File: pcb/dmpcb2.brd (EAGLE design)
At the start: 100 x 100 mm, 70 parts, among them IC1 7805DT, IC2 L293D, IC4 LM358D, IC5 LM358D, J7 SJ-3523-SMT-TR, Q1 IRF530, Q2 IRF530

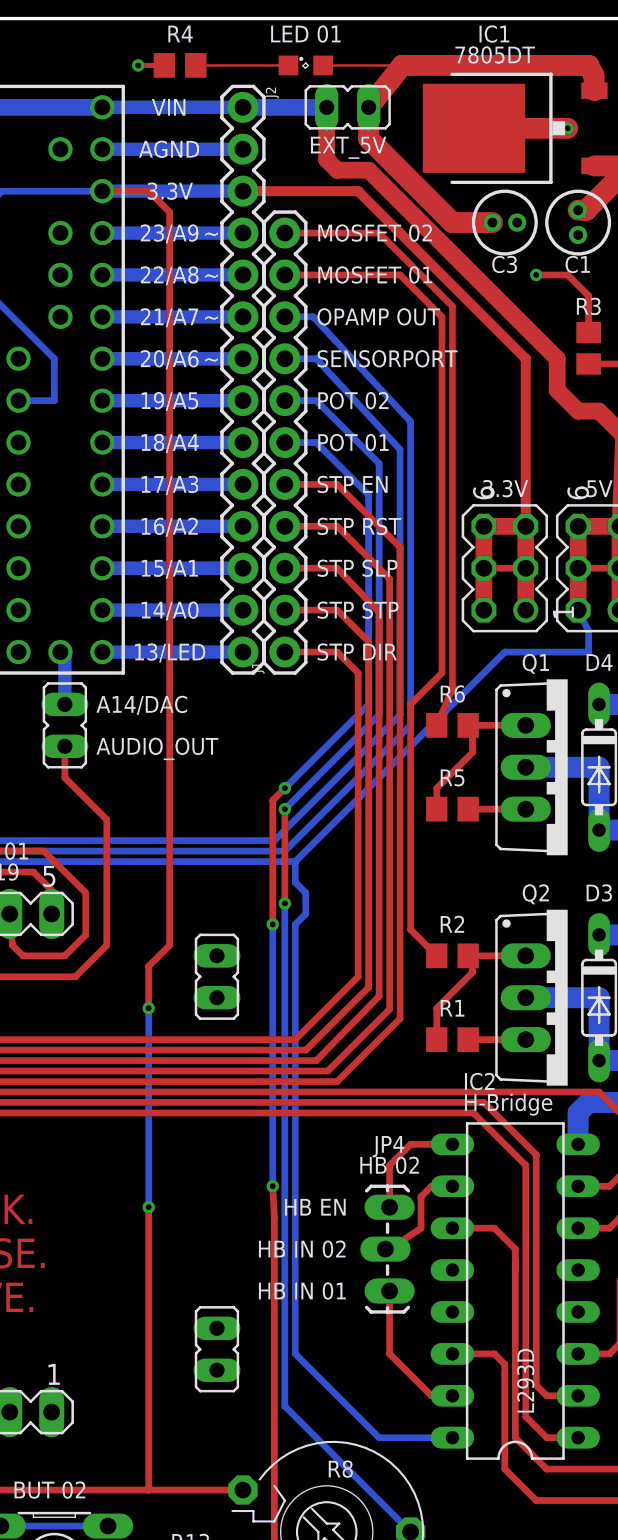
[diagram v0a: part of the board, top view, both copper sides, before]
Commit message: fixed some wire stubs
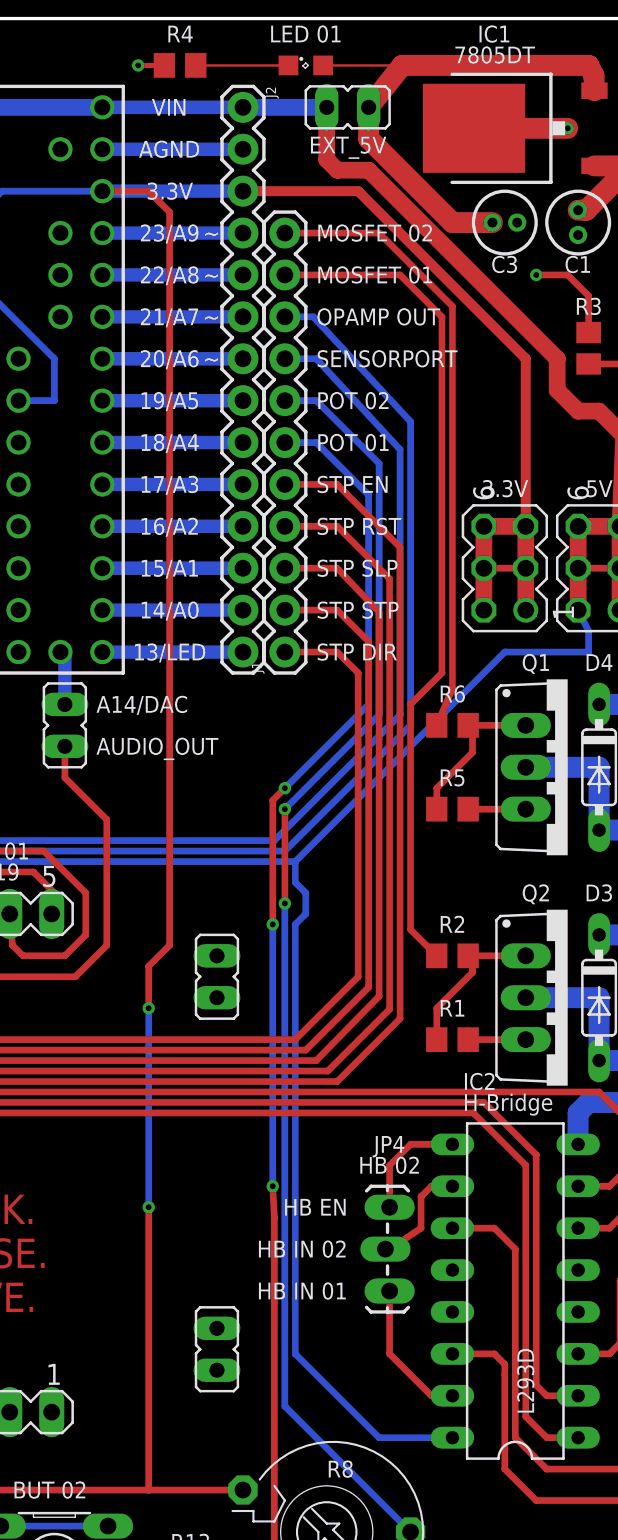
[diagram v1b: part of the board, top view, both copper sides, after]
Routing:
- net +5V: track 359.2 -> 358.0 mm
- net N$12: track 29.5 -> 28.8 mm
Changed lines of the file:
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@@
 <wire x1="89.756784375" y1="74.708215625" x2="89.756784375" y2="74.67648125" width="1.016" layer="1"/>
 <wire x1="89.756784375" y1="74.67648125" x2="89.535" y2="69.215" width="1.016" layer="1"/>
-<wire x1="71.755" y1="94.615" x2="71.755" y2="93.345" width="1.016" layer="1"/>
 <wire x1="89.535" y1="69.215" x2="89.535" y2="66.675" width="1.016" layer="1"/>
 <contactref element="5V" pad="6"/>
@@
 <wire x1="85.725" y1="79.375" x2="74.295" y2="90.805" width="1.016" layer="1"/>
 <wire x1="72.39" y1="90.805" x2="71.755" y2="91.44" width="1.016" layer="1"/>
+<wire x1="74.295" y1="90.805" x2="72.39" y2="90.805" width="1.016" layer="1"/>
 <wire x1="71.755" y1="91.44" x2="71.755" y2="94.615" width="1.016" layer="1"/>
-<wire x1="74.295" y1="90.805" x2="72.39" y2="90.805" width="1.016" layer="1"/>
 </signal>
 <signal name="MM92">
@@
 <wire x1="55.245" y1="79.375" x2="50.8" y2="83.82" width="0.4064" layer="16"/>
 <wire x1="50.8" y1="83.82" x2="47.99" y2="83.82" width="0.4064" layer="16"/>
-<wire x1="58.15" y1="89.535" x2="58.42" y2="89.535" width="0.4064" layer="1"/>
 <wire x1="62.23" y1="43.815" x2="60.96" y2="42.545" width="0.4064" layer="1"/>
 <wire x1="60.96" y1="42.545" x2="60.96" y2="40.005" width="0.4064" layer="1"/>
@@
 <wire x1="81.28" y1="66.675" x2="83.82" y2="66.675" width="0.4064" layer="1"/>
 <wire x1="60.96" y1="89.535" x2="62.23" y2="88.265" width="0.4064" layer="1"/>
+<wire x1="62.23" y1="88.265" x2="62.23" y2="43.815" width="0.4064" layer="1"/>
 <wire x1="58.15" y1="89.535" x2="60.96" y2="89.535" width="0.4064" layer="1"/>
-<wire x1="62.23" y1="88.265" x2="62.23" y2="43.815" width="0.4064" layer="1"/>
 </signal>
 <signal name="N$16">
@@
 <signal name="N$12">
 <contactref element="IC2" pad="11"/>
-<wire x1="83.185" y1="24.765" x2="83.185" y2="24.13" width="0.4064" layer="1"/>
-<wire x1="83.185" y1="24.13" x2="83.185" y2="13.97" width="0.4064" layer="1"/>
+<wire x1="83.185" y1="25.4" x2="83.185" y2="13.97" width="0.4064" layer="1"/>
 <wire x1="83.185" y1="13.97" x2="85.09" y2="12.065" width="0.4064" layer="1"/>
 <wire x1="85.09" y1="12.065" x2="89.535" y2="12.065" width="0.4064" layer="1"/>
@@
 <wire x1="79.375" y1="26.67" x2="81.915" y2="26.67" width="0.4064" layer="1"/>
 <wire x1="81.915" y1="26.67" x2="83.185" y2="25.4" width="0.4064" layer="1"/>
-<wire x1="83.185" y1="25.4" x2="83.185" y2="24.13" width="0.4064" layer="1"/>
 </signal>
 <signal name="H-BRIDGE_B_EN">

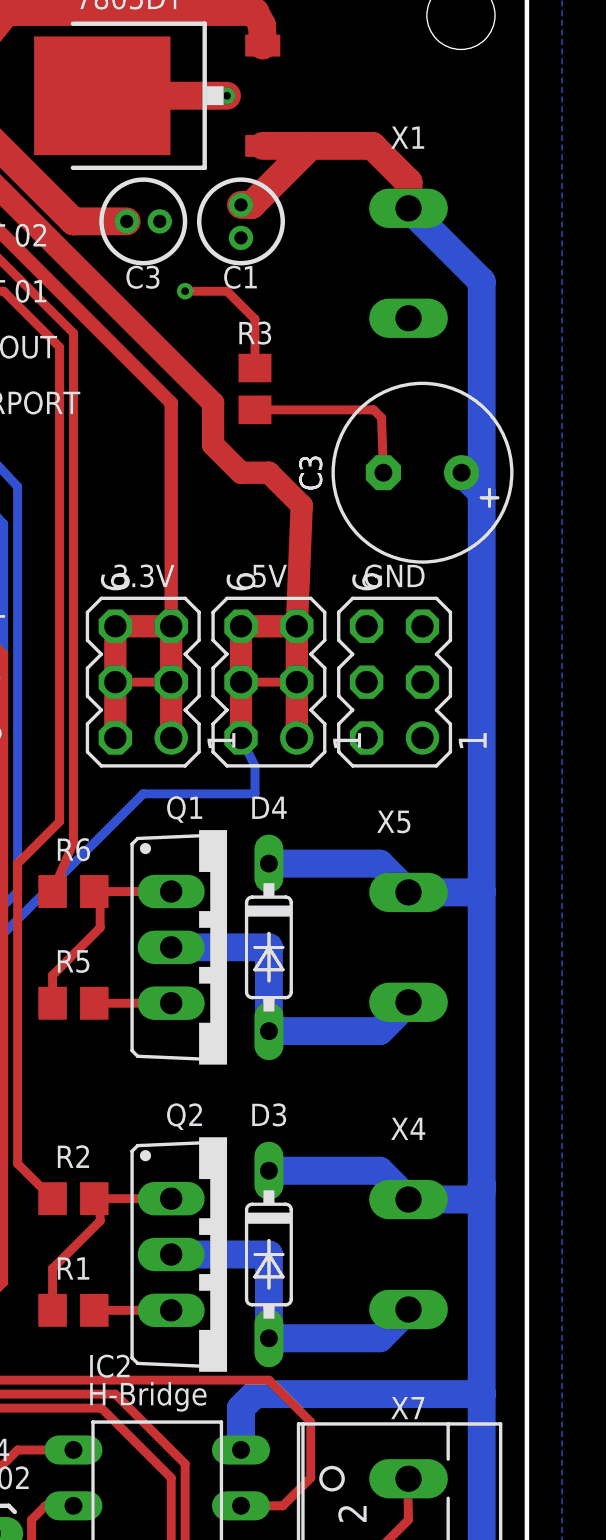
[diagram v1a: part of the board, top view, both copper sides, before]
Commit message: fixed mirrored AKLs
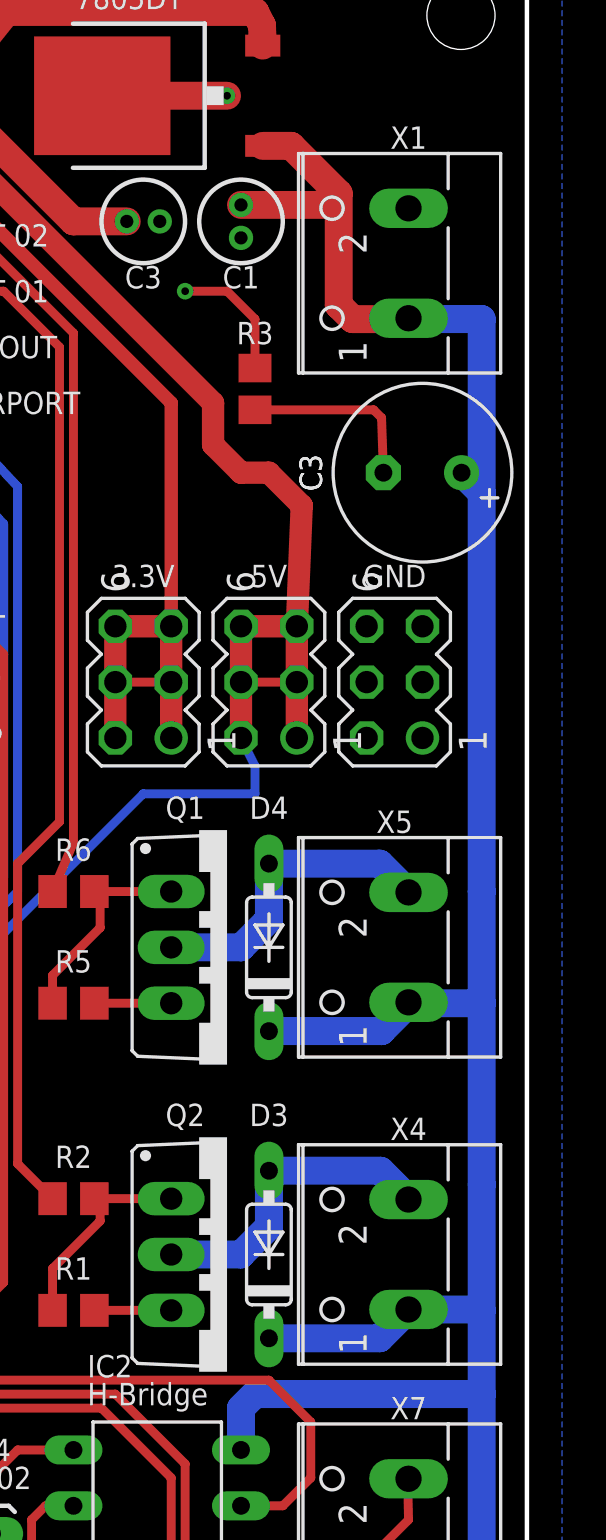
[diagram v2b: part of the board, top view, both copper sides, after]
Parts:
- turned D3 to 90 degrees
- turned D4 to 90 degrees
- flipped X1 to the top, turned to 90 degrees
- flipped X4 to the top, turned to 90 degrees
- flipped X5 to the top, turned to 90 degrees
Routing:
- net V+: track 221.1 -> 222.2 mm
- net M2: track 15.1 -> 14.4 mm
- net M1: track 15.1 -> 14.4 mm
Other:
- board text added: "B2"

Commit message: ver 2
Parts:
- moved 14/DAC 3.59 mm to (58.4, 54.6)
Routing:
- net BETTERAUDIOOUT: track 82.6 -> 79.0 mm
- net N$55: track 3.29 -> 6.88 mm
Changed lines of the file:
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@@
 <text x="70.485" y="99.06" size="1.016" layer="25" align="center">LED 01</text>
 <text x="62.865" y="99.06" size="1.016" layer="25" align="center">R4</text>
-<text x="50.165" y="49.53" size="1.016" layer="25" align="center">DISPLAY 01</text>
-<text x="50.165" y="48.26" size="1.016" layer="25" align="center">MAX7219</text>
+<text x="46.355" y="48.895" size="1.016" layer="25">DISPLAY 01</text>
+<text x="46.355" y="47.625" size="1.016" layer="25">MAX7219</text>
 <text x="19.685" y="98.425" size="1.016" layer="25" font="vector" align="center">J7</text>
 <text x="9.525" y="88.265" size="1.016" layer="25" font="vector" align="center">R19</text>
@@
 <text x="92.075" y="83.185" size="1.016" layer="26" rot="MR0" align="center-left">GND</text>
 <text x="92.075" y="88.265" size="1.016" layer="26" rot="MR0" align="center-left">+</text>
+<text x="46.99" y="51.435" size="1.778" layer="1">BLINK.
+SENSE.
+MOVE.</text>
+<text x="46.99" y="51.435" size="1.778" layer="29">BLINK.
+SENSE.
+MOVE.</text>
 </plain>
 <attributes>
@@
 <attribute name="VALUE" x="64.643" y="95.885" size="0.6096" layer="27" font="vector" ratio="20" rot="R270"/>
 </element>
-<element name="14/DAC" library="jumper" library_urn="urn:adsk.eagle:library:252" package="JP1" package3d_urn="urn:adsk.eagle:package:15455/1" value="" x="55.88" y="57.15" smashed="yes" rot="R180">
-<attribute name="POPULARITY" value="61" x="55.88" y="57.15" size="1.778" layer="27" rot="R180" display="off"/>
-<attribute name="VALUE" x="52.959" y="59.69" size="1.27" layer="27" ratio="10" rot="R270"/>
+<element name="14/DAC" library="jumper" library_urn="urn:adsk.eagle:library:252" package="JP1" package3d_urn="urn:adsk.eagle:package:15455/1" value="" x="58.42" y="54.61" smashed="yes" rot="R180">
+<attribute name="POPULARITY" value="61" x="58.42" y="54.61" size="1.778" layer="27" rot="R180" display="off"/>
+<attribute name="VALUE" x="55.499" y="57.15" size="1.27" layer="27" ratio="10" rot="R270"/>
 </element>
 <element name="J1" library="SparkFun-Connectors" package="1X11" value="" x="69.215" y="61.595" smashed="yes" rot="R90">
@@
 <contactref element="TEENSY3.2" pad="RESET/DAC"/>
 <contactref element="14/DAC" pad="1"/>
-<wire x1="55.61" y1="61.595" x2="55.88" y2="61.325" width="0.8128" layer="16"/>
-<wire x1="55.88" y1="61.325" x2="55.88" y2="58.42" width="0.8128" layer="16"/>
+<wire x1="58.42" y1="56.88" x2="55.61" y2="59.69" width="0.8128" layer="16"/>
+<wire x1="55.61" y1="61.595" x2="55.61" y2="59.69" width="0.8128" layer="16"/>
+<wire x1="58.42" y1="56.88" x2="58.42" y2="55.88" width="0.8128" layer="16"/>
 </signal>
 <signal name="PIN6">
@@
 <contactref element="R17" pad="E"/>
 <contactref element="14/DAC" pad="2"/>
-<wire x1="55.88" y1="55.88" x2="55.88" y2="53.975" width="0.4064" layer="1"/>
-<wire x1="55.88" y1="53.975" x2="58.42" y2="51.435" width="0.4064" layer="1"/>
-<wire x1="58.42" y1="51.435" x2="58.42" y2="43.815" width="0.4064" layer="1"/>
+<wire x1="58.42" y1="53.34" x2="58.42" y2="43.815" width="0.4064" layer="1"/>
 <wire x1="44.45" y1="41.91" x2="30.48" y2="55.745303125" width="0.4064" layer="1"/>
 <wire x1="30.48" y1="55.745303125" x2="30.48" y2="65.405" width="0.4064" layer="1"/>
@@
 </signals>
 <mfgpreviewcolors>
-<mfgpreviewcolor name="soldermaskcolor" color="0xC8FFFF00"/>
+<mfgpreviewcolor name="soldermaskcolor" color="0xC8AAFF00"/>
 <mfgpreviewcolor name="silkscreencolor" color="0xFFFEFEFE"/>
 <mfgpreviewcolor name="backgroundcolor" color="0xFF282828"/>
@@
 <mfgpreviewcolor name="substratecolor" color="0xFF786E46"/>
 </mfgpreviewcolors>
-<errors>
-</errors>
 </board>
 </drawing>

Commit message: issues added and fixed
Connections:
- removed net N$19: S1.1, S1.2
- removed net N$21: S2.1, S2.2
- net 3.3V: now also S1.1, S1.2, S2.1, S2.2
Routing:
- net 3.3V: track 224.6 -> 243.5 mm
- net N$21: track 6.50 -> 0.00 mm
- net N$19: track 6.50 -> 0.00 mm
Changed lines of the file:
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@@
 <?xml version="1.0" encoding="utf-8"?>
 <!DOCTYPE eagle SYSTEM "eagle.dtd">
-<eagle version="9.4.2">
+<eagle version="9.5.2">
 <drawing>
 <settings>
-<setting alwaysvectorfont="yes"/>
+<setting alwaysvectorfont="no"/>
 <setting verticaltext="up"/>
 </settings>
@@
 <wire x1="33.02" y1="5.715" x2="33.02" y2="8.255" width="0.4064" layer="1"/>
 <wire x1="33.02" y1="8.255" x2="35.56" y2="10.795" width="0.4064" layer="1"/>
-<wire x1="35.56" y1="10.795" x2="60.96" y2="10.795" width="0.4064" layer="1"/>
+<wire x1="35.56" y1="10.795" x2="58.42" y2="10.795" width="0.4064" layer="1"/>
+<wire x1="58.42" y1="10.795" x2="60.96" y2="10.795" width="0.4064" layer="1"/>
 <wire x1="60.96" y1="10.795" x2="66.675" y2="10.795" width="0.4064" layer="1"/>
 <wire x1="47.99" y1="61.595" x2="47.99" y2="83.82" width="0.4064" layer="16"/>
@@
 <wire x1="62.23" y1="88.265" x2="62.23" y2="43.815" width="0.4064" layer="1"/>
 <wire x1="58.15" y1="89.535" x2="60.96" y2="89.535" width="0.4064" layer="1"/>
+<contactref element="S1" pad="1"/>
+<contactref element="S1" pad="2"/>
+<wire x1="41.8338" y1="8.6106" x2="48.26" y2="8.6106" width="0.4064" layer="16"/>
+<contactref element="S2" pad="1"/>
+<contactref element="S2" pad="2"/>
+<wire x1="48.26" y1="8.6106" x2="48.3362" y2="8.6106" width="0.4064" layer="16"/>
+<wire x1="51.9938" y1="8.6106" x2="58.4962" y2="8.6106" width="0.4064" layer="16"/>
+<wire x1="58.4962" y1="8.6106" x2="58.4962" y2="10.7188" width="0.4064" layer="1"/>
+<wire x1="58.4962" y1="10.7188" x2="58.42" y2="10.795" width="0.4064" layer="1"/>
+<wire x1="51.9938" y1="8.6106" x2="48.3362" y2="8.6106" width="0.4064" layer="16"/>
 </signal>
 <signal name="N$16">
@@
 <wire x1="27.305" y1="66.675" x2="26.67" y2="67.31" width="0.4064" layer="16"/>
 </signal>
-<signal name="N$19">
-<contactref element="S1" pad="1"/>
-<contactref element="S1" pad="2"/>
-<wire x1="41.8338" y1="8.6106" x2="48.3362" y2="8.6106" width="0.4064" layer="16"/>
-</signal>
-<signal name="N$21">
-<contactref element="S2" pad="1"/>
-<contactref element="S2" pad="2"/>
-<wire x1="51.9938" y1="8.6106" x2="58.4962" y2="8.6106" width="0.4064" layer="16"/>
-</signal>
 <signal name="MAX7219CLK">
